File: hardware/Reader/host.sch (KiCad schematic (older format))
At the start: 6 parts

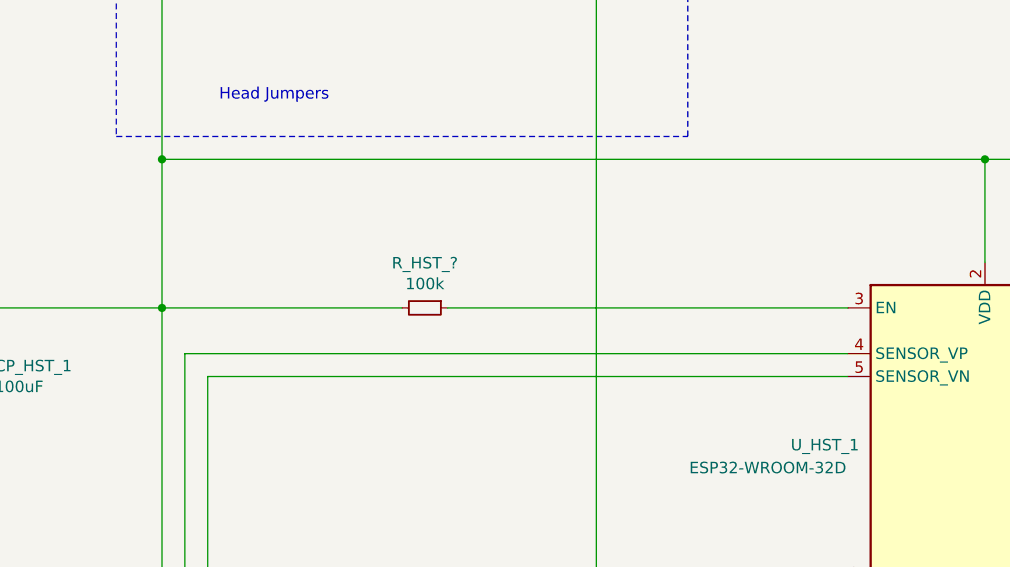
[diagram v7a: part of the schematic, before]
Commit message: Fixed numerous bugs in design for Reader Schematic and PCB
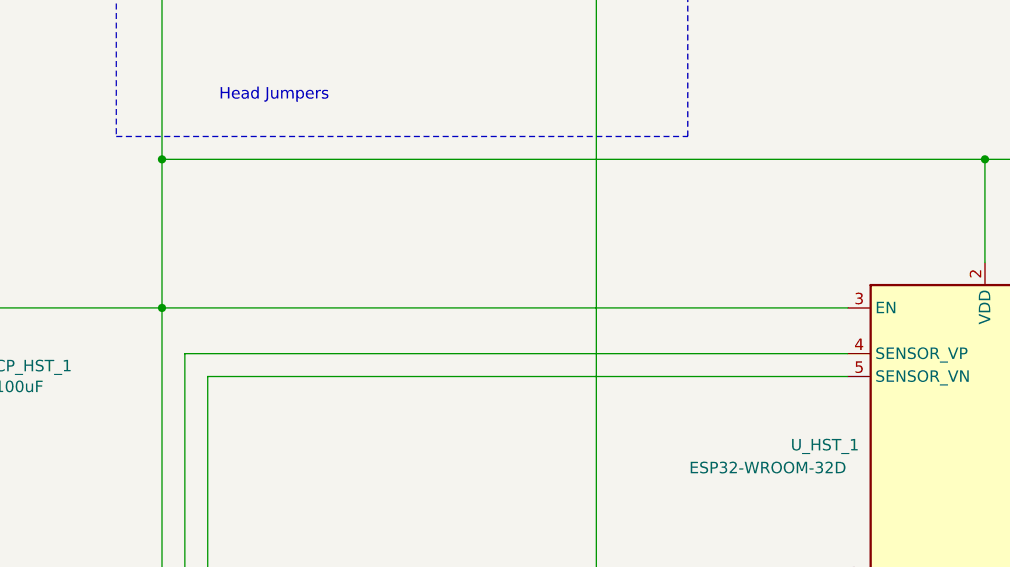
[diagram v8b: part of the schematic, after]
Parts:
- removed R_HST_?: 100k, footprints:RESC1608X55N, symbol Device:R_Small
- CP_HST_1: footprint (none) -> footprints:UCB0J101MCL1GS; Manufacturer (none) -> Nichicon; Part Name (none) -> UCB0J101MCL1GS; Vendor (none) -> DigiKey Canada; digikeypn (none) -> 493-9357-1-ND
- J_HST_1, J_HST_2: Part Name (none) -> 4157
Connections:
- net +3V3: now also U_HST_1.3 (EN)
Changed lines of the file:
@@
 $Descr USLetter 11000 8500
 encoding utf-8
-Sheet 18 19
+Sheet 13 19
 Title "CANnect Reader | Host"
 Date "2020-11-19"
@@
 $EndComp
 $Comp
-L power:GND #PWR?
+L power:GND #PWR0109
 U 1 1 5FBAC756
 P 6550 2000
-F 0 "#PWR?" H 6550 1750 50  0001 C CNN
+F 0 "#PWR0109" H 6550 1750 50  0001 C CNN
 F 1 "GND" H 6555 1827 50  0000 C CNN
 F 2 "" H 6550 2000 50  0001 C CNN
@@
 F 5 "Adafruit Industries LLC" H 8650 5700 50  0001 C CNN "Manufacturer"
 F 6 "1528-2929-ND" H 8650 5700 50  0001 C CNN "digikeypn"
+F 7 "4157" H 8650 5700 50  0001 C CNN "Part Name"
 	1    8650 5700
 	0    1    1    0
@@
 F 5 "Adafruit Industries LLC" H 3500 5700 50  0001 C CNN "Manufacturer"
 F 6 "1528-2929-ND" H 3500 5700 50  0001 C CNN "digikeypn"
+F 7 "4157" H 3500 5700 50  0001 C CNN "Part Name"
 	1    3500 5700
 	0    1    1    0
@@
 	6200 3750 8950 3750
 $Comp
-L power:+3.3V #PWR?
+L power:+3.3V #PWR0110
 U 1 1 5FBD4973
 P 2000 1100
-F 0 "#PWR?" H 2000 950 50  0001 C CNN
+F 0 "#PWR0110" H 2000 950 50  0001 C CNN
 F 1 "+3.3V" H 2015 1273 50  0000 C CNN
 F 2 "" H 2000 1100 50  0001 C CNN
@@
 $EndComp
 $Comp
-L power:GND #PWR?
+L power:GND #PWR0111
 U 1 1 5FBD4DBB
 P 3900 1100
-F 0 "#PWR?" H 3900 850 50  0001 C CNN
+F 0 "#PWR0111" H 3900 850 50  0001 C CNN
 F 1 "GND" H 3905 927 50  0000 C CNN
 F 2 "" H 3900 1100 50  0001 C CNN
@@
 $EndComp
 Wire Wire Line
-	3250 2650 5000 2650
-Wire Wire Line
 	6300 2000 6550 2000
 Wire Wire Line
@@
 	2000 2650 2000 5550
 Wire Wire Line
-	2000 2650 3050 2650
-Wire Wire Line
 	2000 1100 2000 2000
 Wire Wire Line
@@
 	3900 5400 3900 5550
 $Comp
-L power:GND #PWR?
+L power:GND #PWR0112
 U 1 1 5FD0C84B
 P 1150 3250
-F 0 "#PWR?" H 1150 3000 50  0001 C CNN
+F 0 "#PWR0112" H 1150 3000 50  0001 C CNN
 F 1 "GND" H 1155 3077 50  0000 C CNN
 F 2 "" H 1150 3250 50  0001 C CNN
@@
 Wire Wire Line
 	1150 2650 2000 2650
-$Comp
-L Device:R_Small R_HST_?
-U 1 1 5FD1041C
-P 3150 2650
-F 0 "R_HST_?" V 2954 2650 50  0000 C CNN
-F 1 "100k" V 3045 2650 50  0000 C CNN
-F 2 "footprints:RESC1608X55N" H 3150 2650 50  0001 C CNN
-F 3 "https://www.yageo.com/upload/media/product/productsearch/datasheet/rchip/PYu-RT_1-to-0.01_RoHS_L_12.pdf" H 3150 2650 50  0001 C CNN
-	1    3150 2650
-	0    1    1    0
-$EndComp
 $Comp
 L Device:CP CP_HST_1
@@
 F 0 "CP_HST_1" H 1268 2996 50  0000 L CNN
 F 1 "100uF" H 1268 2905 50  0000 L CNN
-F 2 "" H 1188 2800 50  0001 C CNN
-F 3 "~" H 1150 2950 50  0001 C CNN
+F 2 "footprints:UCB0J101MCL1GS" H 1188 2800 50  0001 C CNN
+F 3 "https://www.nichicon.co.jp/english/products/pdfs/e-ucb.pdf" H 1150 2950 50  0001 C CNN
+F 4 "Nichicon" H 1150 2950 50  0001 C CNN "Manufacturer"
+F 5 "UCB0J101MCL1GS" H 1150 2950 50  0001 C CNN "Part Name"
+F 6 "DigiKey Canada" H 1150 2950 50  0001 C CNN "Vendor"
+F 7 "493-9357-1-ND" H 1150 2950 50  0001 C CNN "digikeypn"
 	1    1150 2950
 	1    0    0    -1
@@
 Wire Wire Line
 	1150 2800 1150 2650
+Wire Wire Line
+	2000 2650 5000 2650
 $EndSCHEMATC
